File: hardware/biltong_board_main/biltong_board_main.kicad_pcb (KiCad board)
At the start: 2 copper layers, 100 x 100 mm, 89 parts, among them J1 Altech_AK300-3_P5.00mm, J11 JST_PH_B4B-PH-K_1x04_P2.00mm_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, J12 Conn_02x07_Odd_Even, J2 PinHeader_1x05_P2.54mm_Vertic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, J3 Altech_AK300-2_P5.00mm, J4 Altech_AK300-2_P5.00mm, J5 JST_PH_B4B-PH-K_1x04_P2.00mm_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, J6 JST_PH_B11B-PH-K_1x11_P2.00mm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, J7 JST_PH_B4B-PH-K_1x04_P2.00mm_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, J8 JST_PH_B4B-PH-K_1x04_P2.00mm_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

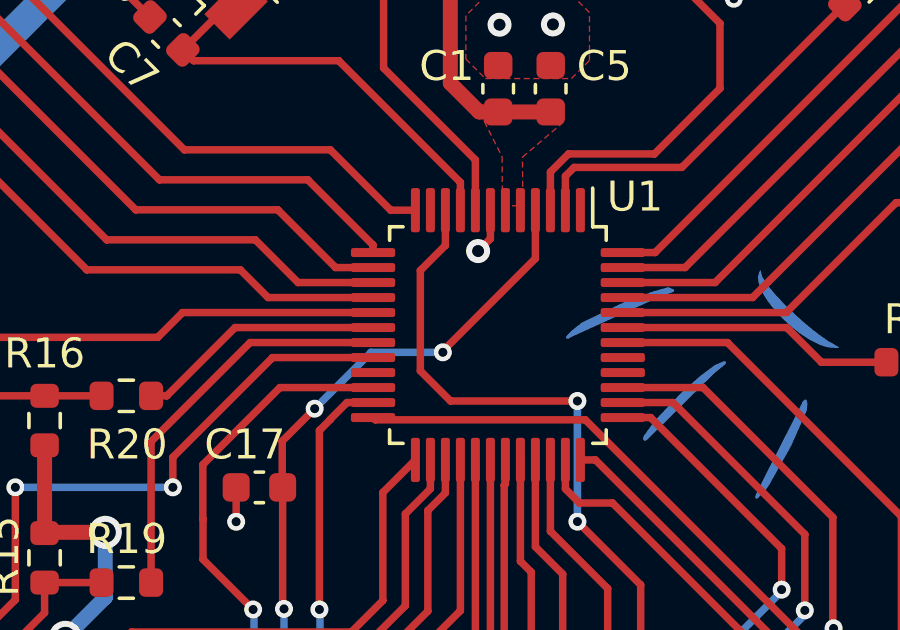
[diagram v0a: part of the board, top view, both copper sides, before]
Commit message: swapped ADC pin
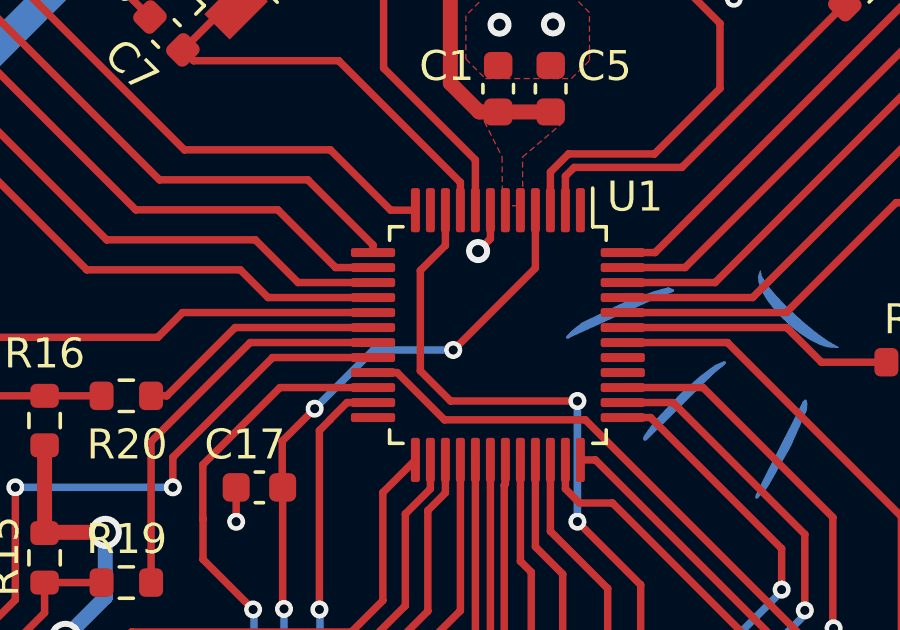
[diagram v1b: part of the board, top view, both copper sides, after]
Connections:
- U1 pad 21: unconnected-(U1-PB2-Pad21) -> /I_SENSE
- U1 pad 24: /I_SENSE -> unconnected-(U1-PB12-Pad24)
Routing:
- net /I_SENSE: track 34.3 -> 34.9 mm

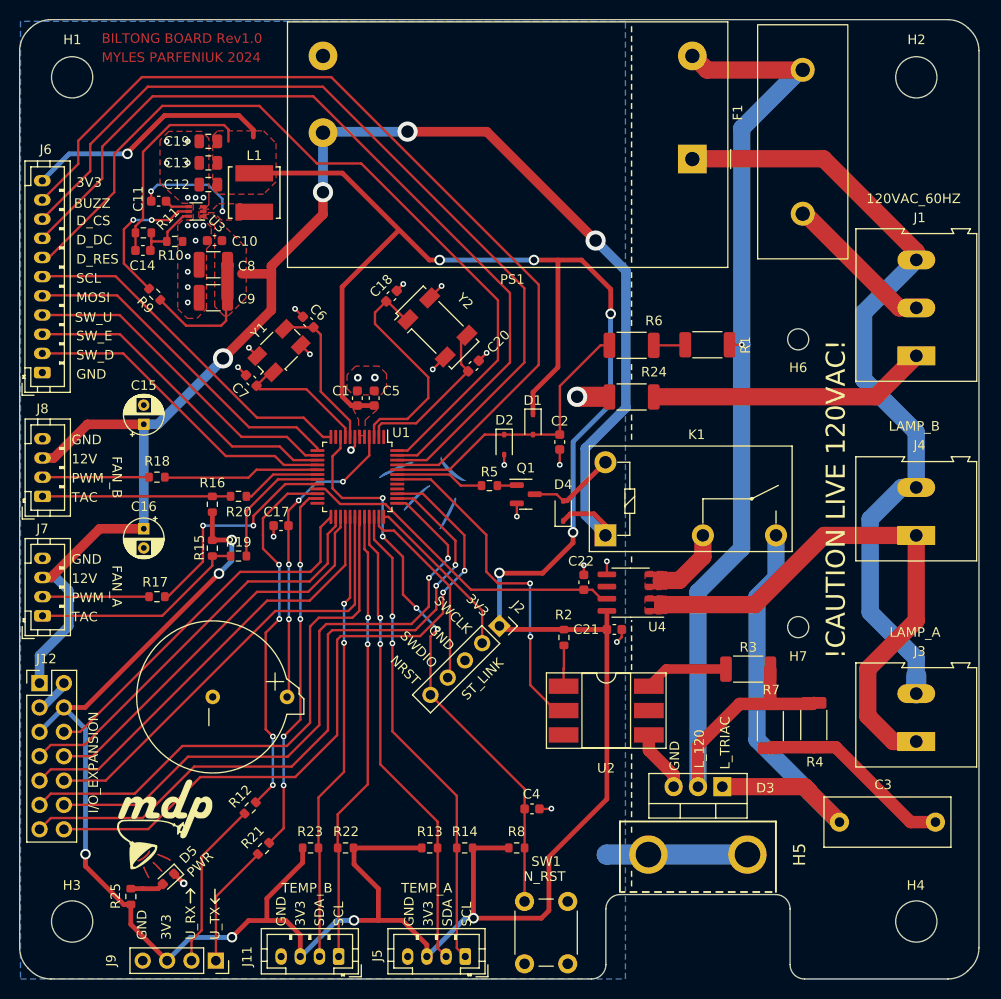
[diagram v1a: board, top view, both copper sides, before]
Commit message: generated BOM, swapped 10u cap size, README.md changes
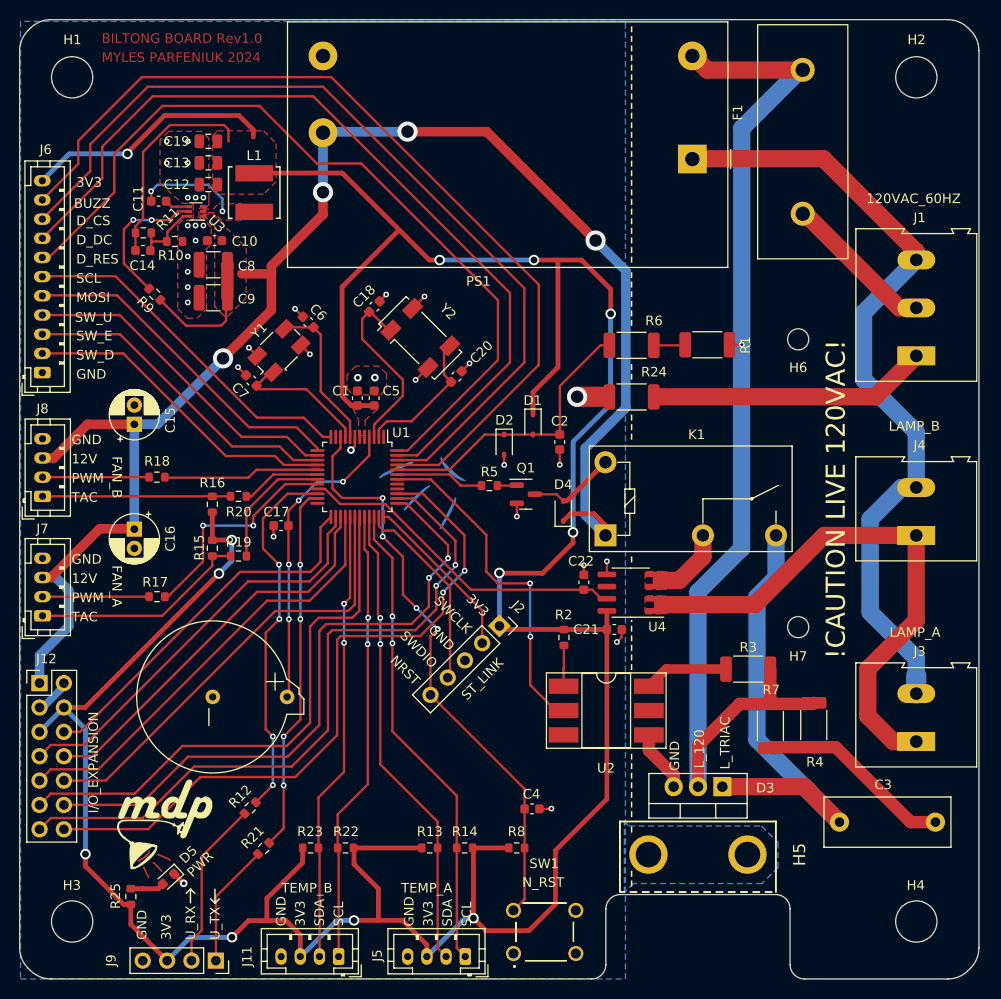
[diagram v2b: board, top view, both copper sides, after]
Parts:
- C15, C16: footprint Capacitor_THT:CP_Radial_D4.0mm_P2.00mm -> Capacitor_THT:CP_Radial_D5.0mm_P2.00mm
- PS1: value IRM-05-12 -> IRM-10-12; footprint BiltongBoardLib:Converter_ACDC_MeanWell_IRM-05-xx_THT_w_model -> BiltongBoardLib:Converter_ACDC_MeanWell_IRM-10-xx_THT_w_model
- SW1: value N_RST -> TL1105BF250Q; footprint BiltongBoardLib:SW_PUSH_6mm_H5mm_4_pin -> BiltongBoardLib:TL1105BF250Q
- U4: value ~ -> NSM2012-10B3R
- moved SW1 7.84 mm to (154.9, 123.2), turned to 90 degrees
- moved C18 2.09 mm to (140.4, 55.8)
- moved C20 2.09 mm to (148.9, 63.1)
- moved Y2 2.09 mm to (145.2, 59.1)
- moved C16 0.98 mm to (115.4, 79.0)
- moved C15 0.98 mm to (115.4, 68.0)
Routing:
- net GND: track 45.1 -> 30.4 mm
- net /OSC32_OUT: track 24.0 -> 19.4 mm
- net /OSC32_IN: track 17.1 -> 14.7 mm
- net /NRST: track 60.2 -> 61.6 mm
- net +3V3: track 371.0 -> 372.1 mm
- net +12V: track 180.3 -> 179.5 mm

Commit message: Fixed HS1 ground issue, missing schematic values, README.md update
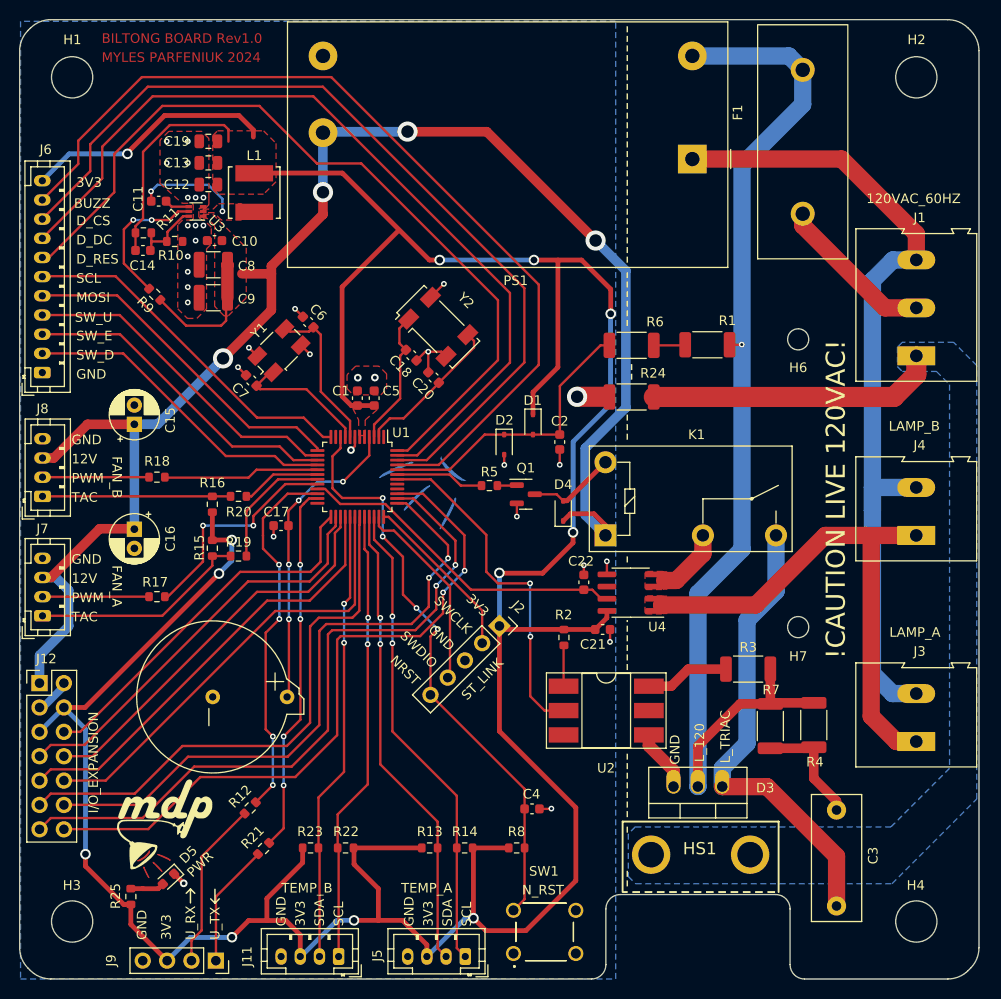
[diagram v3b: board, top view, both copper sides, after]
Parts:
- removed H5: 581002B02500G, BiltongBoardLib:HSINK_581002B02500G
- added HS1: 581002B02500G, BiltongBoardLib:HSINK_581002B02500G, F.Cu at (179.6, 112.9)
- BT1: value CR1220 -> BH-98-1
- D3: footprint Package_TO_SOT_THT:TO-220-3_Vertical -> BiltongBoardLib:TO-220-3_Vertical_long_pads
- D5: value LED -> 150060VS7500
- F1: value Fuse -> 696106003002
- moved C3 10.4 mm to (188.6, 108.3), turned to -90 degrees
- moved C18 6.36 mm to (144.2, 60.8), turned to -45 degrees
- moved C20 2.38 mm to (146.6, 63.2), turned to 135 degrees
- moved Y2 2.20 mm to (147.0, 57.9)
- moved C21 1.22 mm to (164.2, 89.4)
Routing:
- net Net-(C3-Pad1): track 20.5 -> 12.1 mm
- net /N_120: track 82.8 -> 88.1 mm
- net /OSC32_OUT: track 19.4 -> 14.4 mm
- net /L_TRIAC: track 56.5 -> 53.6 mm
- net Earth: track 28.4 -> 30.3 mm
- net GND: track 30.4 -> 32.2 mm, vias 36 -> 34
- net +3V3: track 372.1 -> 373.5 mm
- net /OSC32_IN: track 14.7 -> 15.9 mm
- net Net-(J1-Pin_2): track 15.9 -> 16.7 mm
- net /TRIAC_TRIG: track 35.8 -> 36.5 mm
- net Net-(K1-Pad2): track 7.62 -> 7.08 mm
- net Net-(D3-A1): track 48.1 -> 48.6 mm
- added copper zone on B.Cu, net Earth

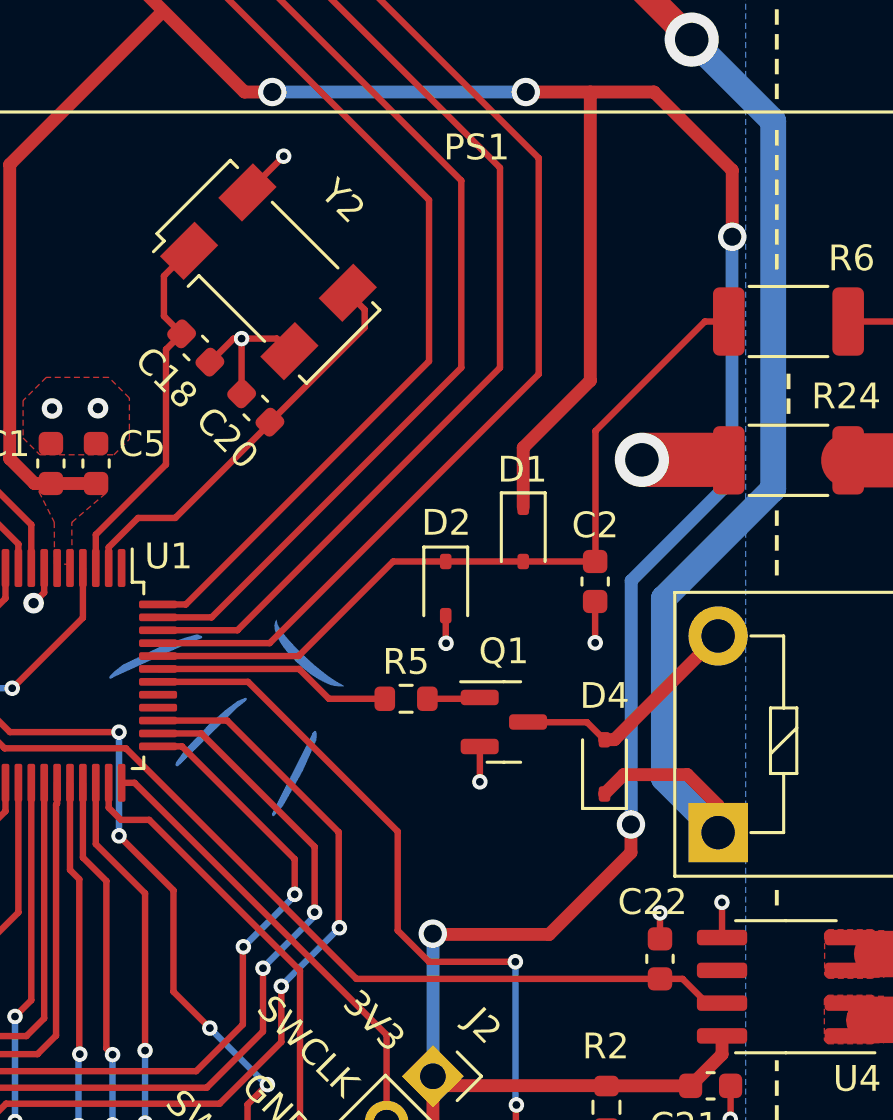
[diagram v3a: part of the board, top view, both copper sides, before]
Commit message: swapped zero cross pin for EXTI_2 line, HS1 recalculation
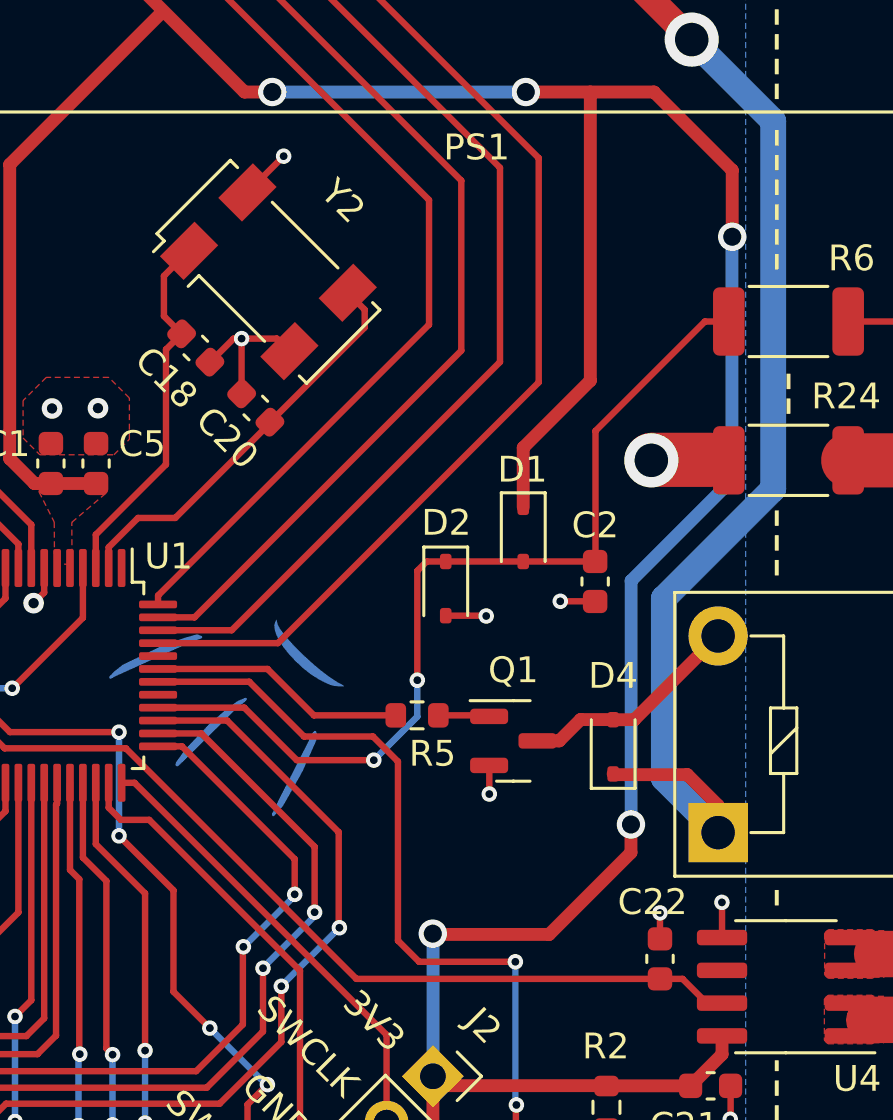
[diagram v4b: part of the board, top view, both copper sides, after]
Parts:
- moved D4 0.85 mm to (160.4, 76.3)
- moved Q1 0.82 mm to (156.5, 76.1)
- moved R5 0.77 mm to (152.8, 75.1)
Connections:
- U1 pad 40: unconnected-(U1-PD2-Pad40) -> /ZERO_CROSS
- U1 pad 44: /ZERO_CROSS -> unconnected-(U1-PB5-Pad44)
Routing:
- net /ZERO_CROSS: track 30.4 -> 36.3 mm, vias 0 -> 2
- net /TRIAC_TRIG: track 36.5 -> 38.3 mm
- net /HEAT_LAMP_EN: track 9.27 -> 9.96 mm
- net /DISP_RES: track 85.4 -> 84.8 mm
- net +12V: track 179.5 -> 178.8 mm
- net Net-(D4-A): track 9.31 -> 8.69 mm
- net GND: track 32.2 -> 31.7 mm

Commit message: Generated gerbers, moved cap trace, cleaned up buck fills
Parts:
- moved U2 0.60 mm to (164.0, 98.2)
- moved R2 0.58 mm to (159.6, 90.3)
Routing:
- net /L_120: track 114.4 -> 108.4 mm
- net Net-(R3-Pad1): track 8.78 -> 9.42 mm

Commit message: RTC oscillator fix, lamp connector new model & footprints
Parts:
- moved C20 1.86 mm to (144.7, 63.5), turned to -45 degrees
- moved C18 1.86 mm to (142.4, 61.2), turned to 135 degrees
- moved Y2 0.68 mm to (147.5, 58.4), turned to 135 degrees
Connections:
- Y2 pad 1: /OSC32_OUT -> /OSC32_IN
- Y2 pad 2: GND -> unconnected-(Y2-Pad2)
- Y2 pad 3: /OSC32_IN -> unconnected-(Y2-Pad3)
- Y2 pad 4: GND -> /OSC32_OUT
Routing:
- net GND: track 31.7 -> 26.3 mm
- net /OSC32_IN: track 15.9 -> 10.9 mm
- net /OSC32_OUT: track 14.4 -> 11.8 mm
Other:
- board text added: "L"
- board text added: "N"

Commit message: Y2 correction, label corrections, new lamp & Vac conn models
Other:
- board text added: "E"
